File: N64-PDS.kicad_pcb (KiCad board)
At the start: 2 copper layers, 35.5 x 59.8 mm, 62 parts, among them J1 USB-C-6P-PWR, J2 I2C_OUT, J3 PWR_OUT, U1 STUSB4500QTR, U2 PTPS55289RYQR, U3 STL6P3LLH6, U4 PTPS55289RYQR

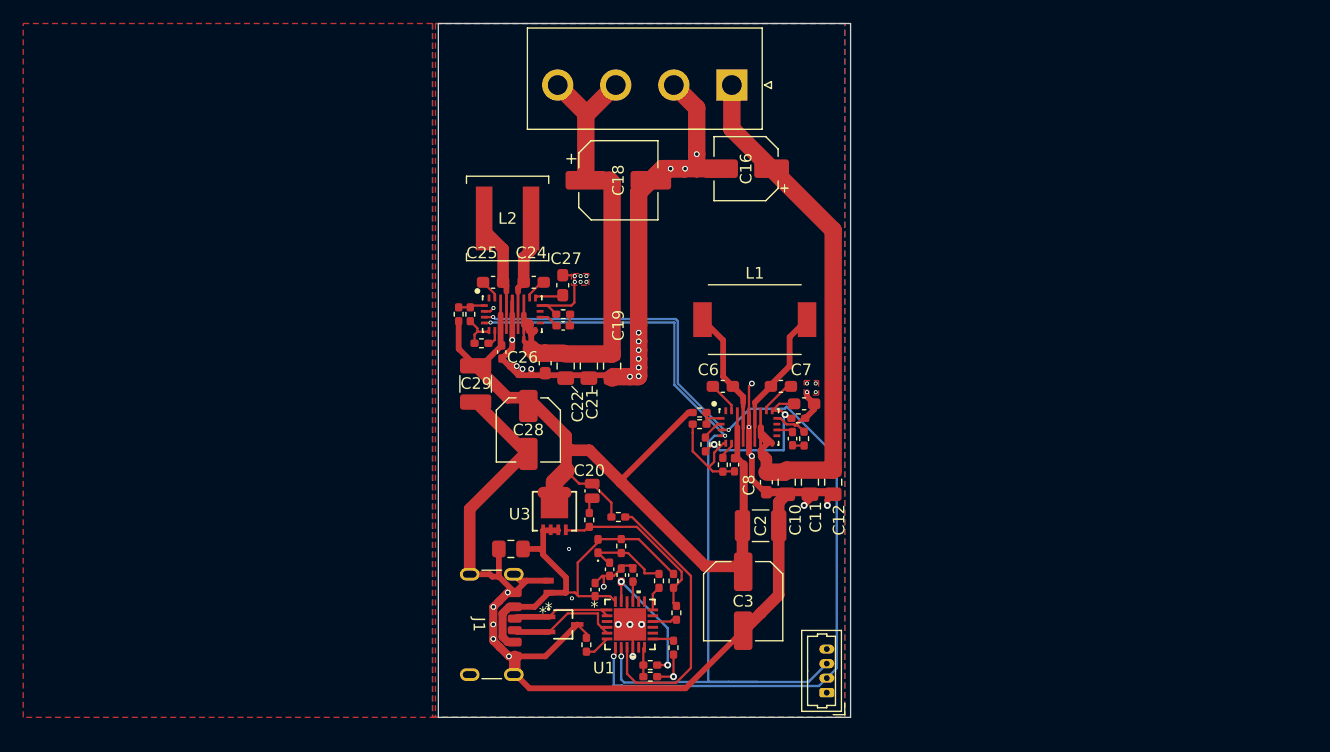
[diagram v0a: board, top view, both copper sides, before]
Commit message: Finalise PCB
Finalise PCB, sent off to JLC for PCB fabrication.
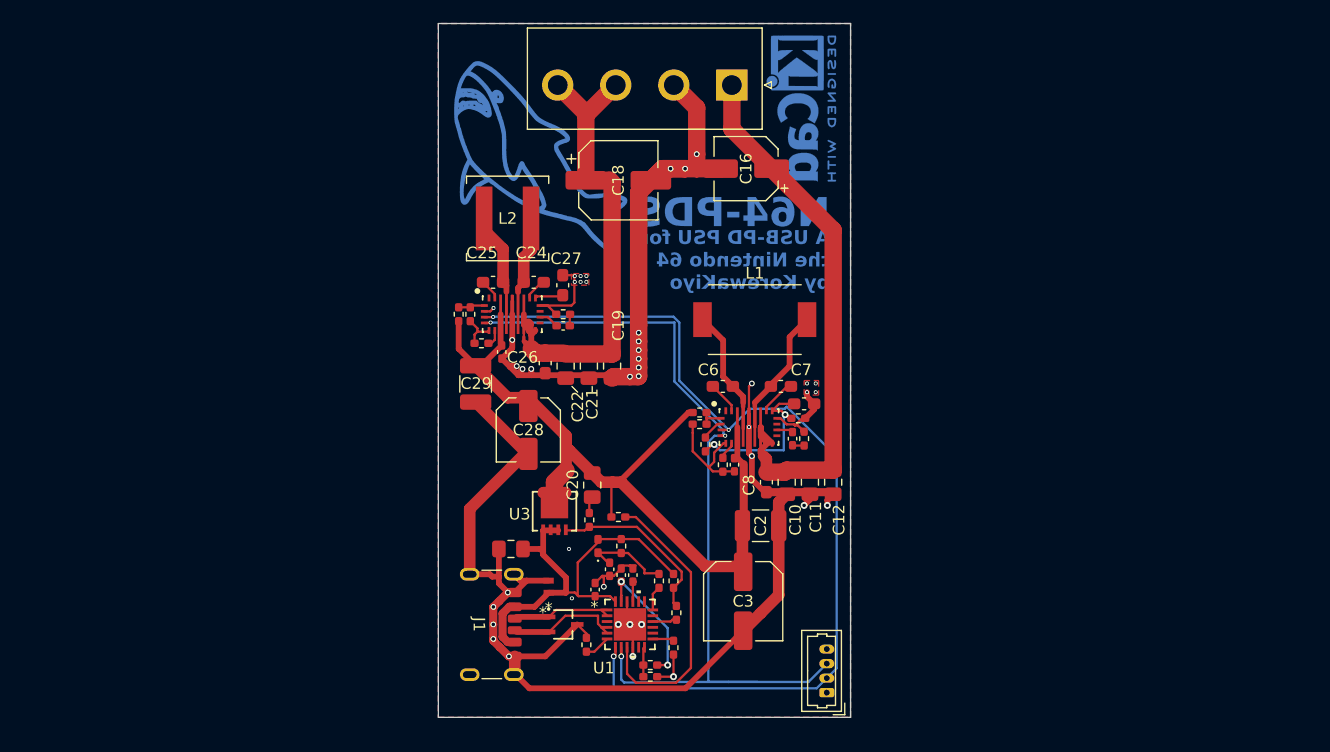
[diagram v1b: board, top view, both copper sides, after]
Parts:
- added G***: LOGO, LOGO, B.Cu at (142.5, 77.5)
- added REF**: KiCad-Logo2_5mm_Copper-exposed, haj:KiCad-Logo2_5mm_Copper-exposed, B.Cu at (165.2, 73.2)
- C20: footprint Capacitor_SMD:C_0504_1310Metric_Pad0.83x1.28mm_HandSolder -> Capacitor_SMD:C_0805_2012Metric_Pad1.18x1.45mm_HandSolder
- moved C20 0.50 mm to (147.2, 105.5)
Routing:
- net VSNK: track 78.1 -> 74.8 mm
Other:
- board text added: "A USB-PD PSU for the Nintendo 64 by KorewaKiyo"
- board text added: "N64-PDS"
- board text removed: "JLCJLCJLCJLC"

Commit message: Oops all redesigns
I did it again, this time smaller, better laid out, and all around maybe gooderer
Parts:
- removed C9: 100n, Capacitor_SMD:C_0402_1005Metric_Pad0.74x0.62mm_HandSolder
- added C32: 4.7n, Capacitor_SMD:C_0402_1005Metric_Pad0.74x0.62mm_HandSolder, F.Cu at (200.4, 100.0)
- added kibuzzard-682FAEAC: G***, kibuzzard-682FAEAC, F.Cu at (201.0, 116.6)
- added kibuzzard-682FAEBC: G***, kibuzzard-682FAEBC, F.Cu at (192.6, 124.4)
- added kibuzzard-682FAEC4: G***, kibuzzard-682FAEC4, F.Cu at (175.5, 112.0)
- added kibuzzard-682FAECA: G***, kibuzzard-682FAECA, F.Cu at (201.6, 112.7)
- added kibuzzard-682FAF07: G***, kibuzzard-682FAF07, F.Cu at (201.1, 74.4)
- added kibuzzard-682FAF0F: G***, kibuzzard-682FAF0F, F.Cu at (176.4, 74.6)
- added kibuzzard-682FAF25: G***, kibuzzard-682FAF25, F.Cu at (191.1, 70.9)
- C20: footprint Capacitor_SMD:C_0805_2012Metric_Pad1.18x1.45mm_HandSolder -> Capacitor_SMD:C_0504_1310Metric_Pad0.83x1.28mm_HandSolder
- R20: value 274 -> 274k
- R9: value 301 -> 56.2k
- U1: footprint STUSB4500:QFN24EP_4X4_STM-M -> Package_DFN_QFN:QFN-24-1EP_4x4mm_P0.5mm_EP2.15x2.15mm_ThermalVias
- moved REF** 57.2 mm to (200.4, 118.4), turned to 90 degrees
- moved D1 48.4 mm to (196.1, 112.6), turned to 180 degrees
- moved C13 47.4 mm to (196.1, 113.5), turned to 0 degrees
- moved R12 46.5 mm to (196.1, 114.4), turned to 0 degrees
- moved R16 43.9 mm to (191.5, 121.0), turned to -90 degrees
- moved G*** 43.9 mm to (185.3, 87.5)
- moved R13 43.2 mm to (196.1, 115.4), turned to 180 degrees
- moved C15 42.0 mm to (192.7, 113.4), turned to 180 degrees
- moved R14 41.9 mm to (196.1, 116.3), turned to 0 degrees
- moved R10 41.9 mm to (196.1, 118.2), turned to 0 degrees
- moved R5 41.7 mm to (193.9, 121.1), turned to -90 degrees
- moved R11 41.6 mm to (196.1, 117.2), turned to 0 degrees
- moved U1 41.5 mm to (192.0, 116.9)
- moved C17 41.5 mm to (188.9, 113.9)
- moved U3 41.4 mm to (185.2, 112.0)
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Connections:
- net DISCH renamed /DISCH
- J2 pad 2: I2C_SCL -> /I2C_SDA
- J2 pad 3: I2C_SDA -> /I2C_SCL
- J2 pad 4: I2C_3V3 -> /VBUS
- R3 pad 1: GND -> Net-(U1-RESET)
- R3 pad 2: Net-(U1-RESET) -> GND
- U1 pad 7: I2C_SCL -> /I2C_SCL
- U1 pad 8: I2C_SDA -> /I2C_SDA
- U2 pad 3: I2C_SCL -> /I2C_SCL
- U2 pad 4: I2C_SDA -> /I2C_SDA
- U4 pad 3: I2C_SCL -> /I2C_SCL
- U4 pad 4: I2C_SDA -> /I2C_SDA
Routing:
- net I2C_SCL: track 82.3 -> 0.00 mm, vias 3 -> 0
- net I2C_SDA: track 76.6 -> 0.00 mm, vias 3 -> 0
- net /I2C_SDA: track 0.00 -> 61.4 mm, vias 0 -> 2
- net /I2C_SCL: track 0.00 -> 50.8 mm, vias 0 -> 2
- net GND: track 198.9 -> 227.6 mm, vias 43 -> 29
- net /DISCH: track 24.5 -> 1.54 mm
- net 3V3O: track 45.0 -> 30.6 mm
- net Net-(U2-SW2): track 11.1 -> 0.40 mm
- net Net-(U2-SW1): track 10.7 -> 0.43 mm
- net Net-(U4-SW2): track 8.71 -> 0.00 mm
- net Net-(U4-SW1): track 8.32 -> 0.00 mm
- net /VBUS: track 36.8 -> 43.1 mm, vias 0 -> 3
- net /VBUS_VS_DISCH: track 7.56 -> 3.72 mm
- net VSNK: track 74.8 -> 71.0 mm, vias 0 -> 4
- net Net-(U3-G): track 15.0 -> 18.2 mm
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- added copper zone on F.Cu, net /VBUS
- added copper zone on F.Cu, net 3V3O
- added copper zone on F.Cu, net Net-(U2-SW1)
- added copper zone on F.Cu, net Net-(U2-SW2)
- added copper zone on F.Cu, net Net-(U4-SW1)
- added copper zone on F.Cu, net Net-(U4-SW2)
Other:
- board size 35.5 x 59.8 mm -> 31 x 57.6 mm

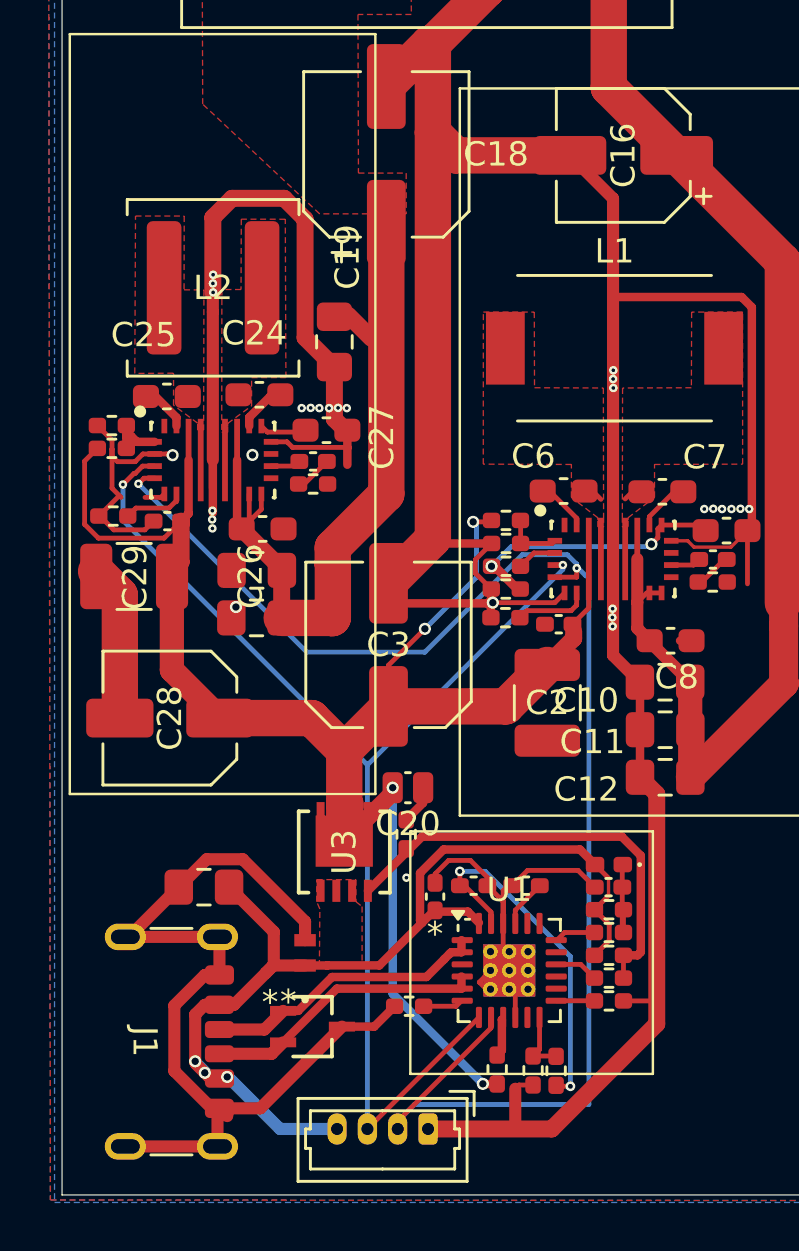
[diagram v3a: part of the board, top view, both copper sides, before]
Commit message: Groundplane tidy up
Tidy up the backside a little to make the ground plane less segmented.
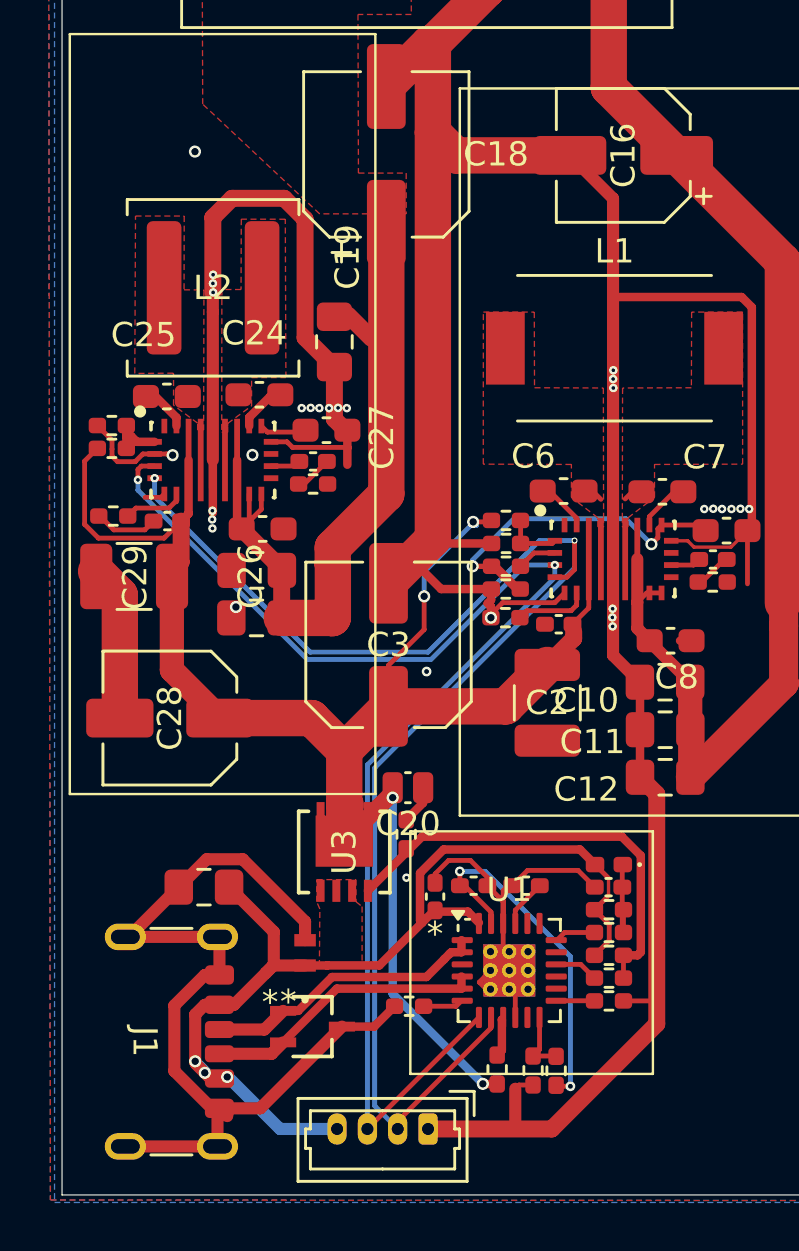
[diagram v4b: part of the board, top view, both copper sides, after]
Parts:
- moved G*** 3.07 mm to (182.4, 88.6)
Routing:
- net /I2C_SCL: track 50.8 -> 56.2 mm
- net GND: track 227.6 -> 222.6 mm, vias 29 -> 31
- net Net-(U2-VCC): track 12.4 -> 15.8 mm
- net /I2C_SDA: track 61.4 -> 59.2 mm
